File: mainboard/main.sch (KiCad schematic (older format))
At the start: 32 parts

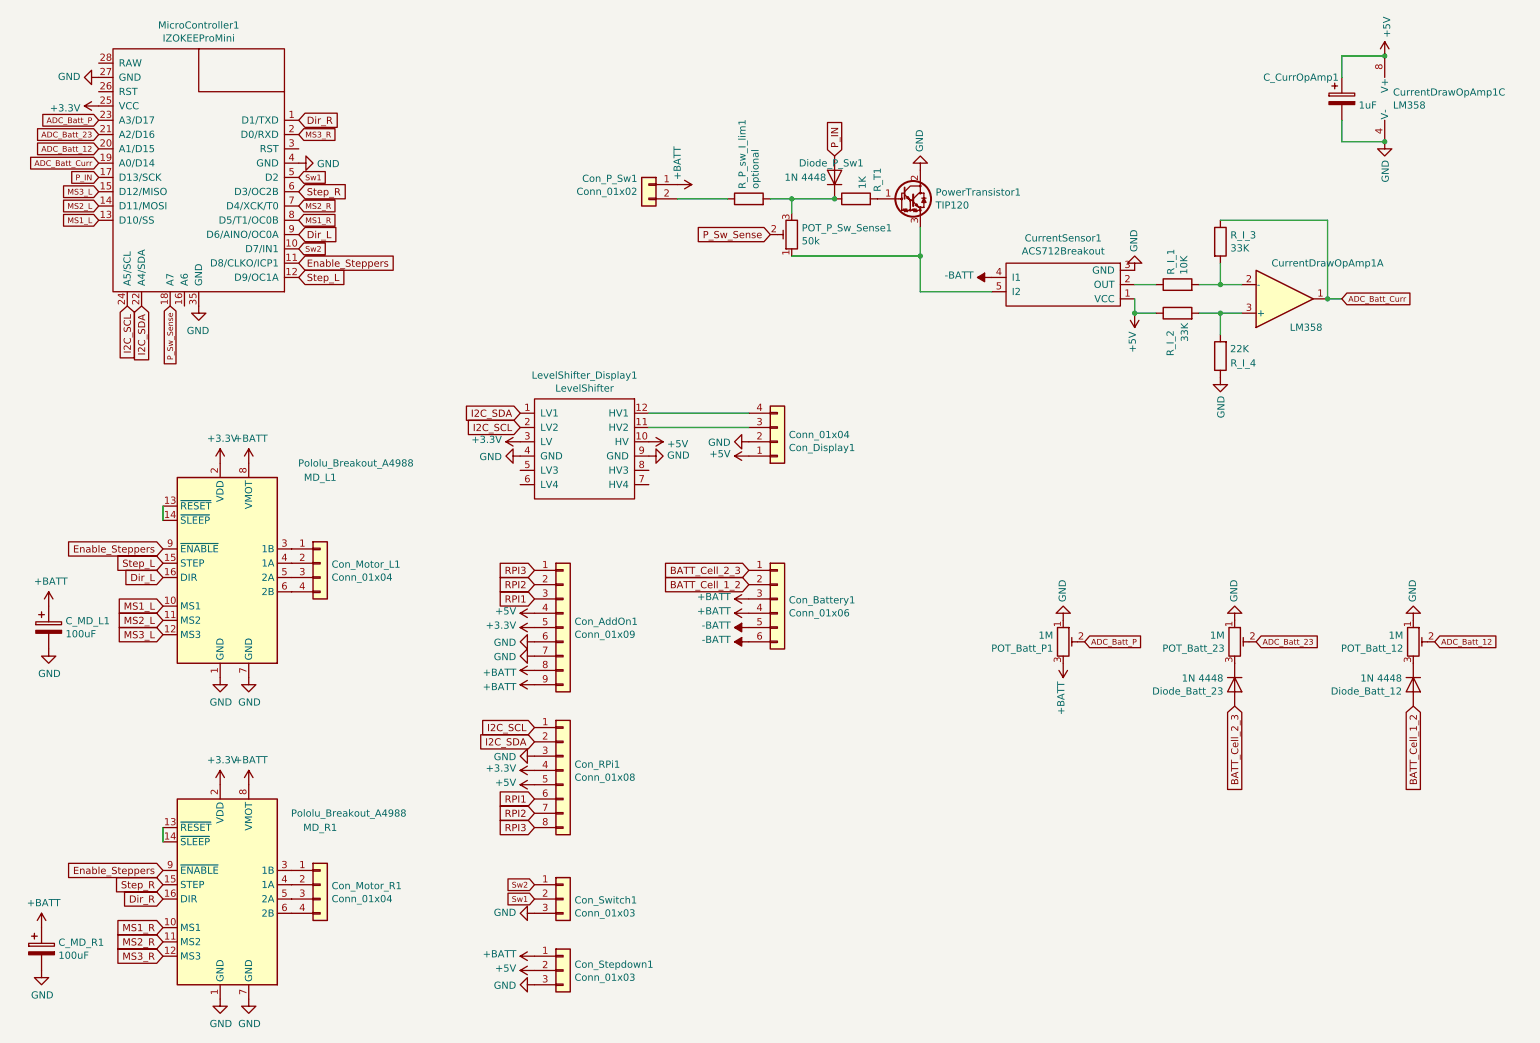
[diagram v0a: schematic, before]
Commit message: New power circuitry and layout
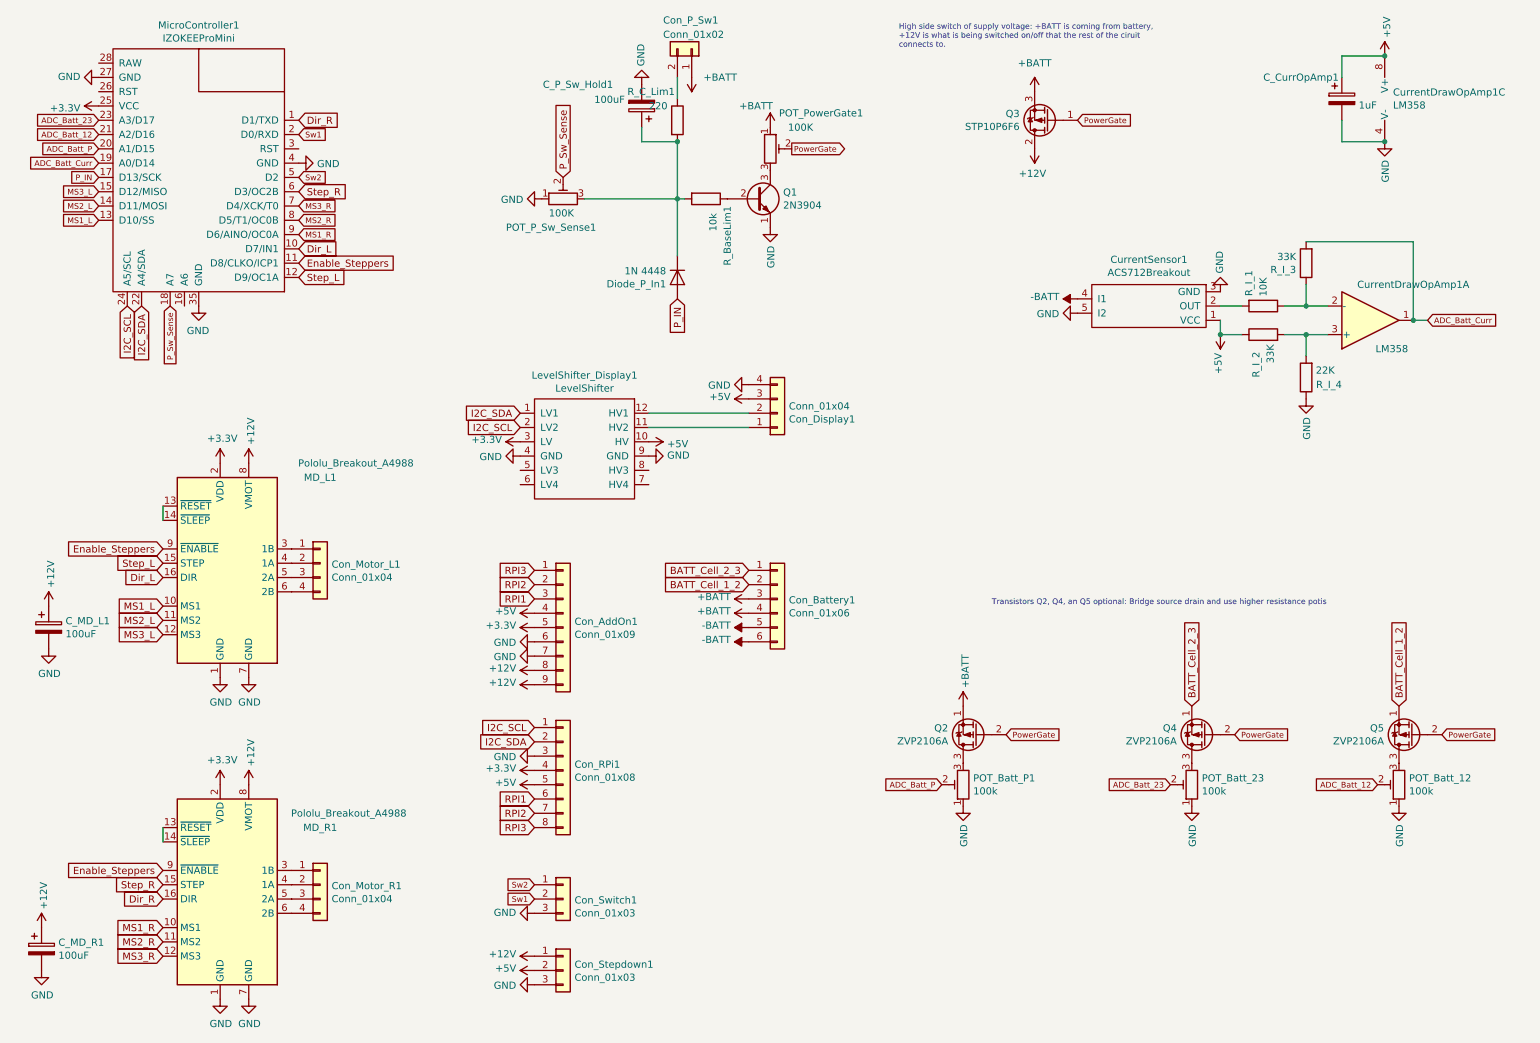
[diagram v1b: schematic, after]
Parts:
- removed Diode_Batt_12, Diode_Batt_23: 1N 4448, Diode_THT:D_T-1_P5.08mm_Horizontal, symbol Device:D
- removed Diode_P_Sw1: 1N 4448, Diode_THT:D_T-1_P10.16mm_Horizontal, symbol Device:D
- removed PowerTransistor1: TIP120, Package_TO_SOT_THT:TO-220-3_Vertical, symbol Transistor_BJT:TIP120
- removed R_P_sw_I_lim1: optional, Resistor_THT:R_Axial_DIN0207_L6.3mm_D2.5mm_P2.54mm_Vertical, symbol Device:R
- removed R_T1: 1K, Resistor_THT:R_Axial_DIN0207_L6.3mm_D2.5mm_P2.54mm_Vertical, symbol Device:R
- added C_P_Sw_Hold1: 100uF, Capacitor_THT:CP_Radial_D5.0mm_P2.50mm, symbol Device:CP
- added Diode_P_In1: 1N 4448, Diode_THT:D_T-1_P5.08mm_Horizontal, symbol Device:D
- added POT_PowerGate1: 100K, Potentiometer_THT:Potentiometer_Bourns_3296W_Vertical, symbol Device:R_POT_TRIM
- added Q1: 2N3904, Package_TO_SOT_THT:TO-92_Inline_Wide, symbol Transistor_BJT:2N3904
- added Q2, Q4, Q5: ZVP2106A, Package_TO_SOT_THT:TO-92L_Inline_Wide, symbol Transistor_FET:TP0610L
- added Q3: STP10P6F6, Package_TO_SOT_THT:TO-220-3_Vertical, symbol Transistor_FET:IRF4905
- added R_BaseLim1: 10k, Resistor_THT:R_Axial_DIN0207_L6.3mm_D2.5mm_P2.54mm_Vertical, symbol Device:R
- added R_C_Lim1: 220, Resistor_THT:R_Axial_DIN0207_L6.3mm_D2.5mm_P2.54mm_Vertical, symbol Device:R
- POT_Batt_12, POT_Batt_23, POT_Batt_P1: value 1M -> 100k
- POT_P_Sw_Sense1: value 50k -> 100K
- R_I_1: footprint Resistor_THT:R_Axial_DIN0207_L6.3mm_D2.5mm_P7.62mm_Horizontal -> Resistor_THT:R_Axial_DIN0207_L6.3mm_D2.5mm_P5.08mm_Vertical
- R_I_3, R_I_4: footprint Resistor_THT:R_Axial_DIN0207_L6.3mm_D2.5mm_P2.54mm_Vertical -> Resistor_THT:R_Axial_DIN0207_L6.3mm_D2.5mm_P5.08mm_Vertical
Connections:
- net +5V: now also Con_Display1.3 (Pin_3); no longer Con_Display1.1 (Pin_1)
- net +BATT: now also POT_PowerGate1.1, Q2.1 (S), Q3.3 (S); no longer C_MD_L1.1, C_MD_R1.1, Con_AddOn1.8 (Pin_8), Con_AddOn1.9 (Pin_9), Con_Stepdown1.1 (Pin_1), MD_L1.8 (VMOT), MD_R1.8 (VMOT), POT_Batt_P1.3
- net ADC_Batt_12: now also MicroController1.21 (A2/D16); no longer MicroController1.20 (A1/D15)
- net ADC_Batt_23: now also MicroController1.23 (A3/D17); no longer MicroController1.21 (A2/D16)
- net ADC_Batt_Curr: now also R_I_3.2; no longer R_I_3.1
- net ADC_Batt_P: now also MicroController1.20 (A1/D15); no longer MicroController1.23 (A3/D17)
- net BATT_Cell_1_2: now also Q5.1 (S)
- net BATT_Cell_2_3: now also Q4.1 (S)
- net Dir_L: now also MicroController1.10 (D7/IN1); no longer MicroController1.9 (D6/AINO/OC0A)
- net GND: now also Con_Display1.4 (Pin_4), CurrentSensor1.5 (I2), POT_P_Sw_Sense1.1, C_P_Sw_Hold1.2, Q1.1 (E); no longer Con_Display1.2 (Pin_2)
- net MS1_R: now also MicroController1.9 (D6/AINO/OC0A); no longer MicroController1.8 (D5/T1/OC0B)
- net MS2_R: now also MicroController1.8 (D5/T1/OC0B); no longer MicroController1.7 (D4/XCK/T0)
- net MS3_R: now also MicroController1.7 (D4/XCK/T0); no longer MicroController1.2 (D0/RXD)
- net P_IN: now also Diode_P_In1.2 (A)
- net Sw1: now also MicroController1.2 (D0/RXD); no longer MicroController1.5 (D2)
- net Sw2: now also MicroController1.5 (D2); no longer MicroController1.10 (D7/IN1)
- net at LevelShifter_Display1.11 (HV2): now also Con_Display1.1 (Pin_1); no longer Con_Display1.3 (Pin_3)
- net at LevelShifter_Display1.12 (HV1): now also Con_Display1.2 (Pin_2); no longer Con_Display1.4 (Pin_4)
- net at CurrentSensor1.2 (OUT): now also R_I_1.2; no longer R_I_1.1
- net at Con_P_Sw1.2 (Pin_2): now also R_C_Lim1.1
- net at POT_P_Sw_Sense1.3: now also C_P_Sw_Hold1.1, Diode_P_In1.1 (K), R_BaseLim1.2, R_C_Lim1.2
- net at POT_Batt_23.3: now also Q4.3 (D)
- net at POT_Batt_12.3: now also Q5.3 (D)
- new net: CurrentDrawOpAmp1.2 (-), R_I_1.1, R_I_3.1
- new net: POT_Batt_P1.3, Q2.3 (D)
- new net: Q1.2 (B), R_BaseLim1.1
- new net: POT_PowerGate1.3, Q1.3 (C)
- new net +12V: C_MD_L1.1, C_MD_R1.1, Con_AddOn1.8 (Pin_8), Con_AddOn1.9 (Pin_9), Con_Stepdown1.1 (Pin_1), MD_L1.8 (VMOT), MD_R1.8 (VMOT), Q3.2 (D)
- new net PowerGate: POT_PowerGate1.2, Q2.2 (G), Q3.1 (G), Q4.2 (G), Q5.2 (G)
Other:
- note added: "High side switch of supply voltage: +BATT is coming from battery,\n+12V is what is being switched on/off that the rest of the ciruit\nconnects to."
- note added: "Transistors Q2, Q4, an Q5 optional: Bridge source drain and use higher resistance potis"
- moved on the sheet: Con_Display1, Con_P_Sw1, CurrentDrawOpAmp1A, CurrentSensor1, POT_Batt_12, POT_Batt_23, POT_Batt_P1, POT_P_Sw_Sense1, R_I_1, R_I_2, R_I_3, R_I_4

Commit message: - 200k potis for cell voltage sensing - hints on setting up the trim potis - Better layout of labels on PCB
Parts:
- POT_Batt_12, POT_Batt_23, POT_Batt_P1: value 100k -> 200k
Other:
- note added: "*BEFORE* plugging in the uC, adjust POT_Batt_x so that all ADC voltages are always < 3.3V.\nI recommend hitting 3.3V for 4.5V * [1, 2, 3] respectively.\nKeep in mind that Q5 might not fully open due to high PowerGate voltages."
- note added: "*BEFORE* plugging in the uC, adjust\nPOT_P_Sw_Sense1 so that P_Sw_Sense\nis slightly below 3.3V for +BATT = 12.6V\nand the power button (Con_P_Sw1) pressed."
- note added: "Adjust POT_PowerGate1 so that PowerGate drops\nto < 1V when switched on, otherwise Q5 does not open."
- note removed: "Transistors Q2, Q4, an Q5 optional: Bridge source drain and use higher resistance potis"
- moved on the sheet: POT_Batt_12, POT_Batt_23, POT_Batt_P1, Q2, Q4, Q5
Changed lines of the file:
@@
 Text GLabel 4600 1700 1    50   Input ~ 0
 P_Sw_Sense
-Text GLabel 10300 5950 0    40   Input ~ 0
+Text GLabel 10300 5800 0    40   Input ~ 0
 ADC_Batt_12
-Text GLabel 7250 5950 0    40   Input ~ 0
+Text GLabel 7250 5800 0    40   Input ~ 0
 ADC_Batt_P
-Text GLabel 8850 5950 0    40   Input ~ 0
+Text GLabel 8850 5800 0    40   Input ~ 0
 ADC_Batt_23
 Text GLabel 10650 2700 2    40   Input ~ 0
@@
 	0    1    1    0
 $EndComp
-Text GLabel 9000 5400 1    50   Input ~ 0
+Text GLabel 9000 5250 1    50   Input ~ 0
 BATT_Cell_2_3
-Text GLabel 10450 5400 1    50   Input ~ 0
+Text GLabel 10450 5250 1    50   Input ~ 0
 BATT_Cell_1_2
 $Comp
 L Device:R_POT_TRIM POT_Batt_P1
 U 1 1 5E57EF6D
-P 7400 5950
-F 0 "POT_Batt_P1" H 7330 5904 50  0000 R CNN
-F 1 "100k" H 7330 5995 50  0000 R CNN
-F 2 "Potentiometer_THT:Potentiometer_Bourns_3296W_Vertical" H 7400 5950 50  0001 C CNN
-F 3 "~" H 7400 5950 50  0001 C CNN
-	1    7400 5950
+P 7400 5800
+F 0 "POT_Batt_P1" H 7330 5754 50  0000 R CNN
+F 1 "200k" H 7330 5845 50  0000 R CNN
+F 2 "Potentiometer_THT:Potentiometer_Bourns_3296W_Vertical" H 7400 5800 50  0001 C CNN
+F 3 "~" H 7400 5800 50  0001 C CNN
+	1    7400 5800
 	-1   0    0    1
 $EndComp
@@
 L Device:R_POT_TRIM POT_Batt_23
 U 1 1 5E59E0E2
-P 9000 5950
-F 0 "POT_Batt_23" H 8930 5904 50  0000 R CNN
-F 1 "100k" H 8930 5995 50  0000 R CNN
-F 2 "Potentiometer_THT:Potentiometer_Bourns_3296W_Vertical" H 9000 5950 50  0001 C CNN
-F 3 "~" H 9000 5950 50  0001 C CNN
-	1    9000 5950
+P 9000 5800
+F 0 "POT_Batt_23" H 8930 5754 50  0000 R CNN
+F 1 "200k" H 8930 5845 50  0000 R CNN
+F 2 "Potentiometer_THT:Potentiometer_Bourns_3296W_Vertical" H 9000 5800 50  0001 C CNN
+F 3 "~" H 9000 5800 50  0001 C CNN
+	1    9000 5800
 	-1   0    0    1
 $EndComp
@@
 L Device:R_POT_TRIM POT_Batt_12
 U 1 1 5E59F13C
-P 10450 5950
-F 0 "POT_Batt_12" H 10380 5904 50  0000 R CNN
-F 1 "100k" H 10380 5995 50  0000 R CNN
-F 2 "Potentiometer_THT:Potentiometer_Bourns_3296W_Vertical" H 10450 5950 50  0001 C CNN
-F 3 "~" H 10450 5950 50  0001 C CNN
-	1    10450 5950
+P 10450 5800
+F 0 "POT_Batt_12" H 10380 5754 50  0000 R CNN
+F 1 "200k" H 10380 5845 50  0000 R CNN
+F 2 "Potentiometer_THT:Potentiometer_Bourns_3296W_Vertical" H 10450 5800 50  0001 C CNN
+F 3 "~" H 10450 5800 50  0001 C CNN
+	1    10450 5800
 	-1   0    0    1
 $EndComp
@@
 L power:GND #PWR0128
 U 1 1 5E5BAC0A
-P 10450 6100
-F 0 "#PWR0128" H 10450 5850 50  0001 C CNN
-F 1 "GND" V 10455 5972 50  0000 R CNN
-F 2 "" H 10450 6100 50  0001 C CNN
-F 3 "" H 10450 6100 50  0001 C CNN
-	1    10450 6100
+P 10450 5950
+F 0 "#PWR0128" H 10450 5700 50  0001 C CNN
+F 1 "GND" V 10455 5822 50  0000 R CNN
+F 2 "" H 10450 5950 50  0001 C CNN
+F 3 "" H 10450 5950 50  0001 C CNN
+	1    10450 5950
 	1    0    0    -1
 $EndComp
@@
 L power:GND #PWR0129
 U 1 1 5E5BBA68
-P 9000 6100
-F 0 "#PWR0129" H 9000 5850 50  0001 C CNN
-F 1 "GND" V 9005 5972 50  0000 R CNN
-F 2 "" H 9000 6100 50  0001 C CNN
-F 3 "" H 9000 6100 50  0001 C CNN
-	1    9000 6100
+P 9000 5950
+F 0 "#PWR0129" H 9000 5700 50  0001 C CNN
+F 1 "GND" V 9005 5822 50  0000 R CNN
+F 2 "" H 9000 5950 50  0001 C CNN
+F 3 "" H 9000 5950 50  0001 C CNN
+	1    9000 5950
 	1    0    0    -1
 $EndComp
@@
 L power:+BATT #PWR0139
 U 1 1 5DA4010C
-P 7400 5400
-F 0 "#PWR0139" H 7400 5250 50  0001 C CNN
-F 1 "+BATT" V 7415 5527 50  0000 L CNN
-F 2 "" H 7400 5400 50  0001 C CNN
-F 3 "" H 7400 5400 50  0001 C CNN
-	1    7400 5400
+P 7400 5250
+F 0 "#PWR0139" H 7400 5100 50  0001 C CNN
+F 1 "+BATT" V 7415 5377 50  0000 L CNN
+F 2 "" H 7400 5250 50  0001 C CNN
+F 3 "" H 7400 5250 50  0001 C CNN
+	1    7400 5250
 	1    0    0    -1
 $EndComp
@@
 L power:GND #PWR0127
 U 1 1 5E5B9E5B
-P 7400 6100
-F 0 "#PWR0127" H 7400 5850 50  0001 C CNN
-F 1 "GND" V 7405 5972 50  0000 R CNN
-F 2 "" H 7400 6100 50  0001 C CNN
-F 3 "" H 7400 6100 50  0001 C CNN
-	1    7400 6100
+P 7400 5950
+F 0 "#PWR0127" H 7400 5700 50  0001 C CNN
+F 1 "GND" V 7405 5822 50  0000 R CNN
+F 2 "" H 7400 5950 50  0001 C CNN
+F 3 "" H 7400 5950 50  0001 C CNN
+	1    7400 5950
 	1    0    0    -1
 $EndComp
@@
 L Transistor_FET:TP0610L Q2
 U 1 1 5E9FB931
-P 7500 5600
-F 0 "Q2" H 7705 5554 50  0000 L CNN
-F 1 "ZVP2106A" H 7705 5645 50  0000 L CNN
-F 2 "Package_TO_SOT_THT:TO-92L_Inline_Wide" H 7700 5525 50  0001 L CIN
-F 3 "" H 7500 5600 50  0001 L CNN
-	1    7500 5600
+P 7500 5450
+F 0 "Q2" H 7705 5404 50  0000 L CNN
+F 1 "ZVP2106A" H 7705 5495 50  0000 L CNN
+F 2 "Package_TO_SOT_THT:TO-92L_Inline_Wide" H 7700 5375 50  0001 L CIN
+F 3 "" H 7500 5450 50  0001 L CNN
+	1    7500 5450
 	-1   0    0    1
 $EndComp
@@
 Text GLabel 8200 1300 2    40   Input ~ 0
 PowerGate
-Text GLabel 7700 5600 2    40   Input ~ 0
+Text GLabel 7700 5450 2    40   Input ~ 0
 PowerGate
 $Comp
 L Transistor_FET:TP0610L Q4
 U 1 1 5EA4093C
-P 9100 5600
-F 0 "Q4" H 9305 5554 50  0000 L CNN
-F 1 "ZVP2106A" H 9305 5645 50  0000 L CNN
-F 2 "Package_TO_SOT_THT:TO-92L_Inline_Wide" H 9300 5525 50  0001 L CIN
-F 3 "" H 9100 5600 50  0001 L CNN
-	1    9100 5600
-	-1   0    0    1
-$EndComp
-Text GLabel 9300 5600 2    40   Input ~ 0
+P 9100 5450
+F 0 "Q4" H 9305 5404 50  0000 L CNN
+F 1 "ZVP2106A" H 9305 5495 50  0000 L CNN
+F 2 "Package_TO_SOT_THT:TO-92L_Inline_Wide" H 9300 5375 50  0001 L CIN
+F 3 "" H 9100 5450 50  0001 L CNN
+	1    9100 5450
+	-1   0    0    1
+$EndComp
+Text GLabel 9300 5450 2    40   Input ~ 0
 PowerGate
 $Comp
 L Transistor_FET:TP0610L Q5
 U 1 1 5EA48428
-P 10550 5600
-F 0 "Q5" H 10755 5554 50  0000 L CNN
-F 1 "ZVP2106A" H 10755 5645 50  0000 L CNN
-F 2 "Package_TO_SOT_THT:TO-92L_Inline_Wide" H 10750 5525 50  0001 L CIN
-F 3 "" H 10550 5600 50  0001 L CNN
-	1    10550 5600
-	-1   0    0    1
-$EndComp
-Text GLabel 10750 5600 2    40   Input ~ 0
+P 10550 5450
+F 0 "Q5" H 10755 5404 50  0000 L CNN
+F 1 "ZVP2106A" H 10755 5495 50  0000 L CNN
+F 2 "Package_TO_SOT_THT:TO-92L_Inline_Wide" H 10750 5375 50  0001 L CIN
+F 3 "" H 10550 5450 50  0001 L CNN
+	1    10550 5450
+	-1   0    0    1
+$EndComp
+Text GLabel 10750 5450 2    40   Input ~ 0
 PowerGate
 $Comp
@@
 Text GLabel 1850 2600 3    40   Input ~ 0
 P_Sw_Sense
-Text Notes 7600 4700 0    39   ~ 0
-Transistors Q2, Q4, an Q5 optional: Bridge source drain and use higher resistance potis
 Text Notes 6950 800  0    39   ~ 0
 High side switch of supply voltage: +BATT is coming from battery,\n+12V is what is being switched on/off that the rest of the ciruit\nconnects to.
+Text Notes 6150 1750 0    39   ~ 0
+Adjust POT_PowerGate1 so that PowerGate drops\nto < 1V when switched on, otherwise Q5 does not open.
+Text Notes 6950 6500 0    39   ~ 0
+*BEFORE* plugging in the uC, adjust POT_Batt_x so that all ADC voltages are always < 3.3V.\nI recommend hitting 3.3V for 4.5V * [1, 2, 3] respectively.\nKeep in mind that Q5 might not fully open due to high PowerGate voltages.
+Text Notes 3600 2400 0    39   ~ 0
+*BEFORE* plugging in the uC, adjust\nPOT_P_Sw_Sense1 so that P_Sw_Sense\nis slightly below 3.3V for +BATT = 12.6V\nand the power button (Con_P_Sw1) pressed.
 $EndSCHEMATC
